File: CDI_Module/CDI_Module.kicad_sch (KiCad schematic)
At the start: 5 parts, among them Q1 TIC226

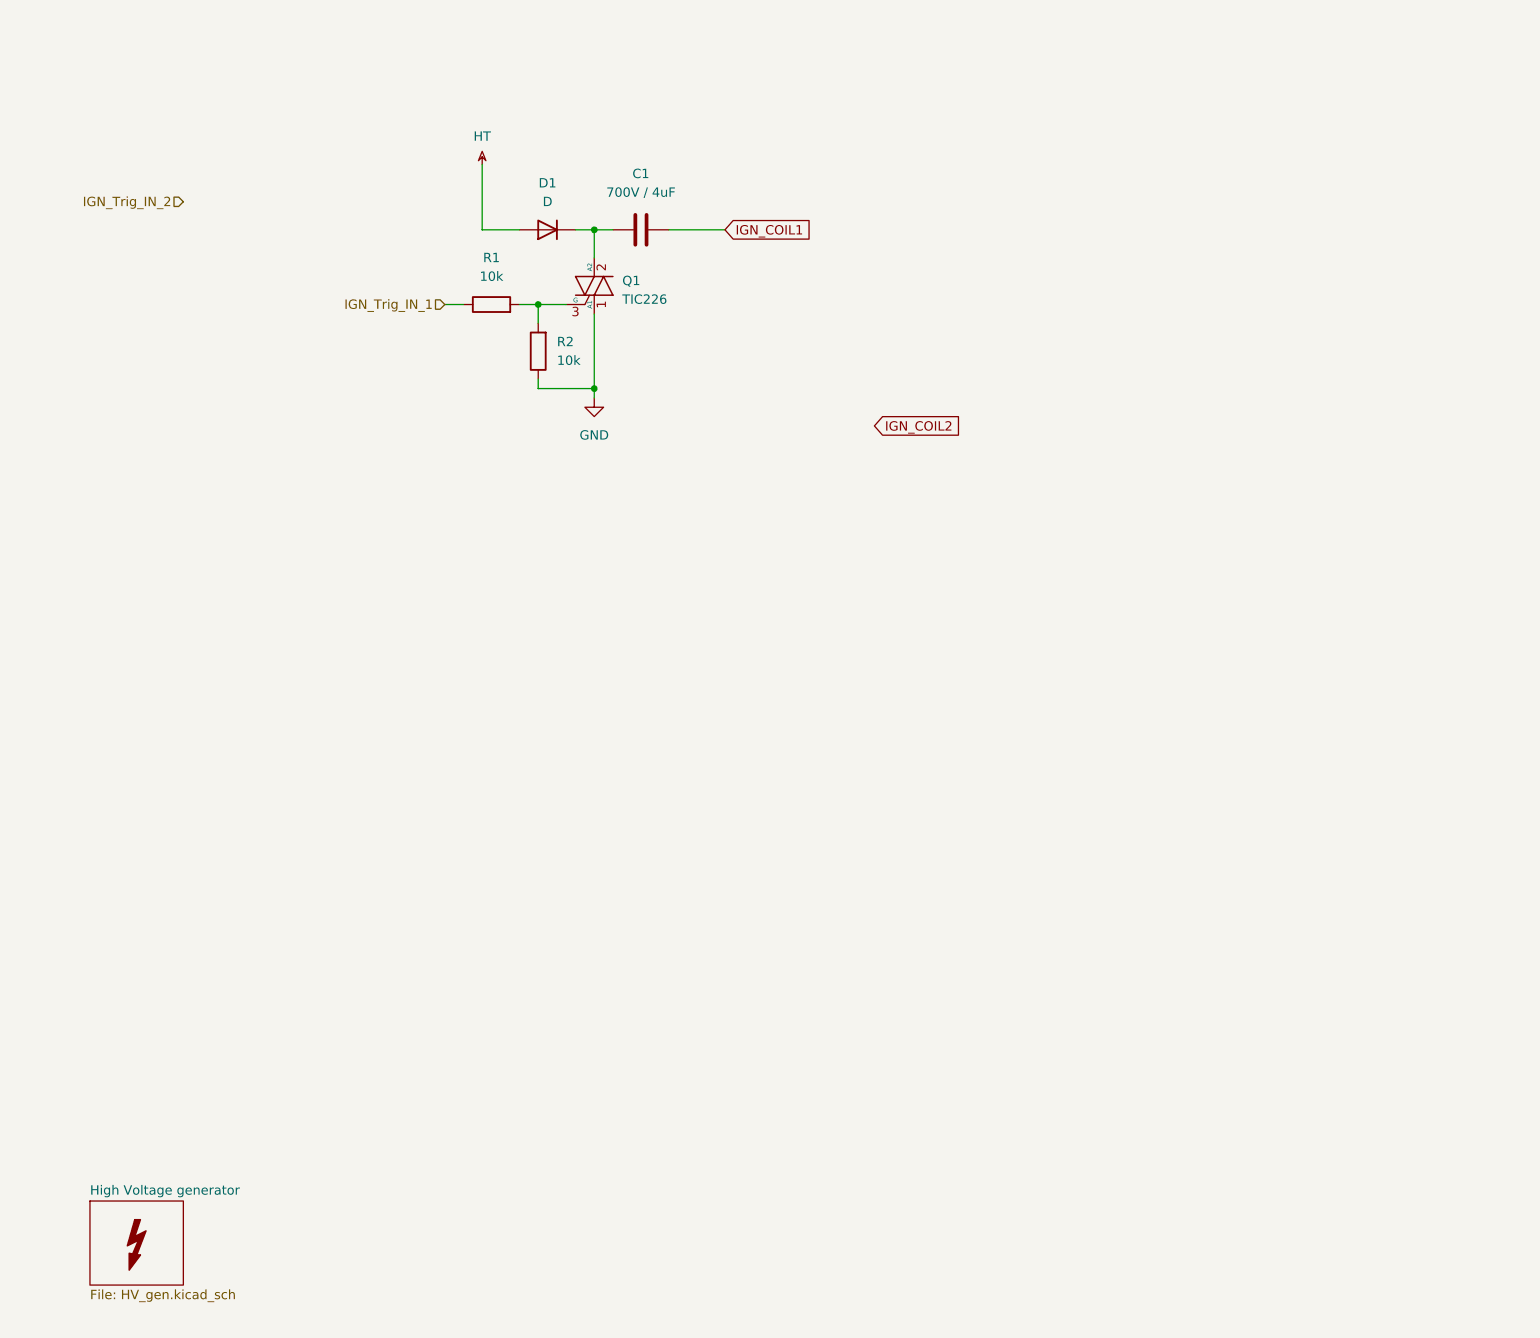
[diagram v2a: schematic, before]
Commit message: Changed Connectors for Molex CMC 48pins Black.
Changed ECU Connector for Molex CMC 48pins Black, for compacity and cost reduction. Designed custom Footprint for this purpose
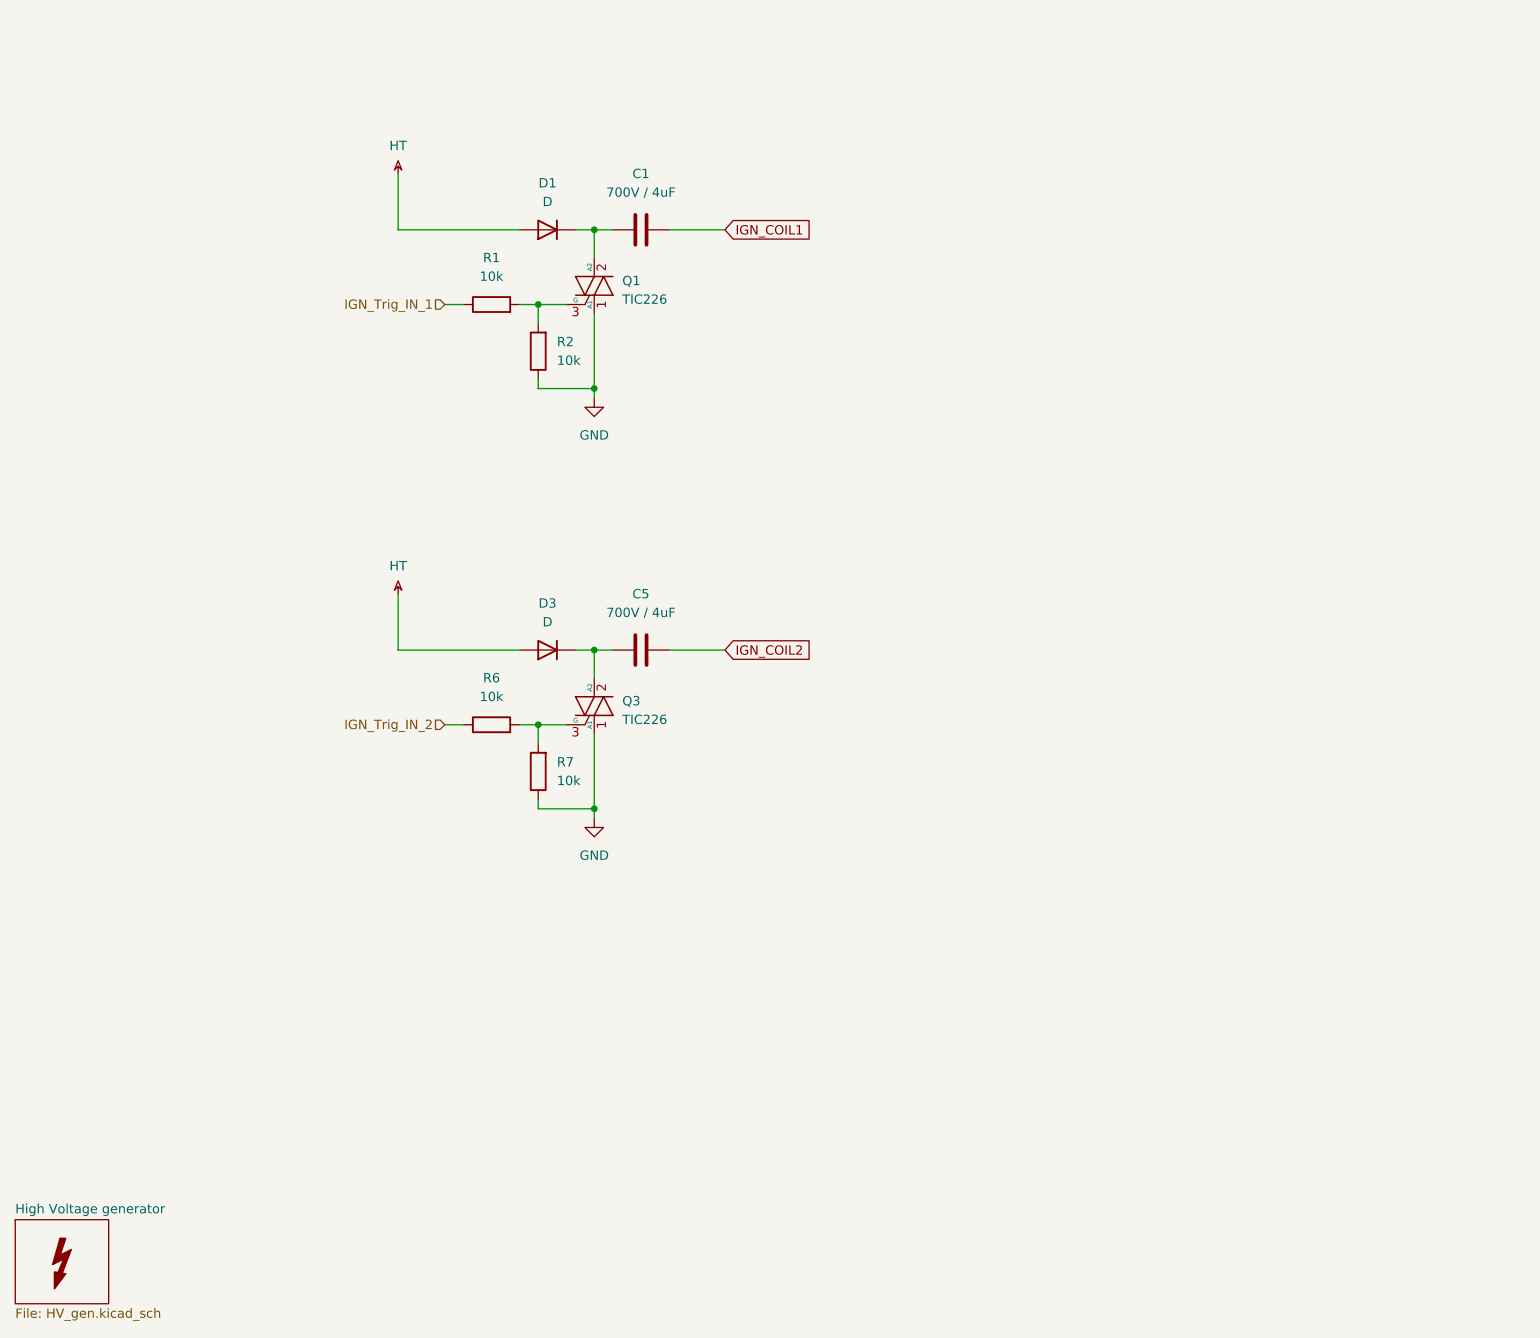
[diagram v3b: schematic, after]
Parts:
- added C5: 700V / 4uF, symbol Device:C
- added D3: D, Diode_SMD:D_0805_2012Metric_Pad1.15x1.40mm_HandSolder, symbol Device:D
- added Q3: TIC226, Package_TO_SOT_THT:TO-220-3_Vertical, symbol Triac_Thyristor:TIC226
- added R6, R7: 10k, Resistor_SMD:R_0603_1608Metric_Pad0.98x0.95mm_HandSolder, symbol Device:R
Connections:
- net GND: now also Q3.1 (A1), R7.1
- net HT: now also D3.2 (A)
- net IGN_COIL2: now also C5.2
- net IGN_Trig_IN_2: now also R6.1
- new net: C5.1, D3.1 (K), Q3.2 (A2)
- new net: Q3.3 (G), R6.2, R7.2

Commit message: Redraw CDI pwr Supply with Boost circuit for 48v output
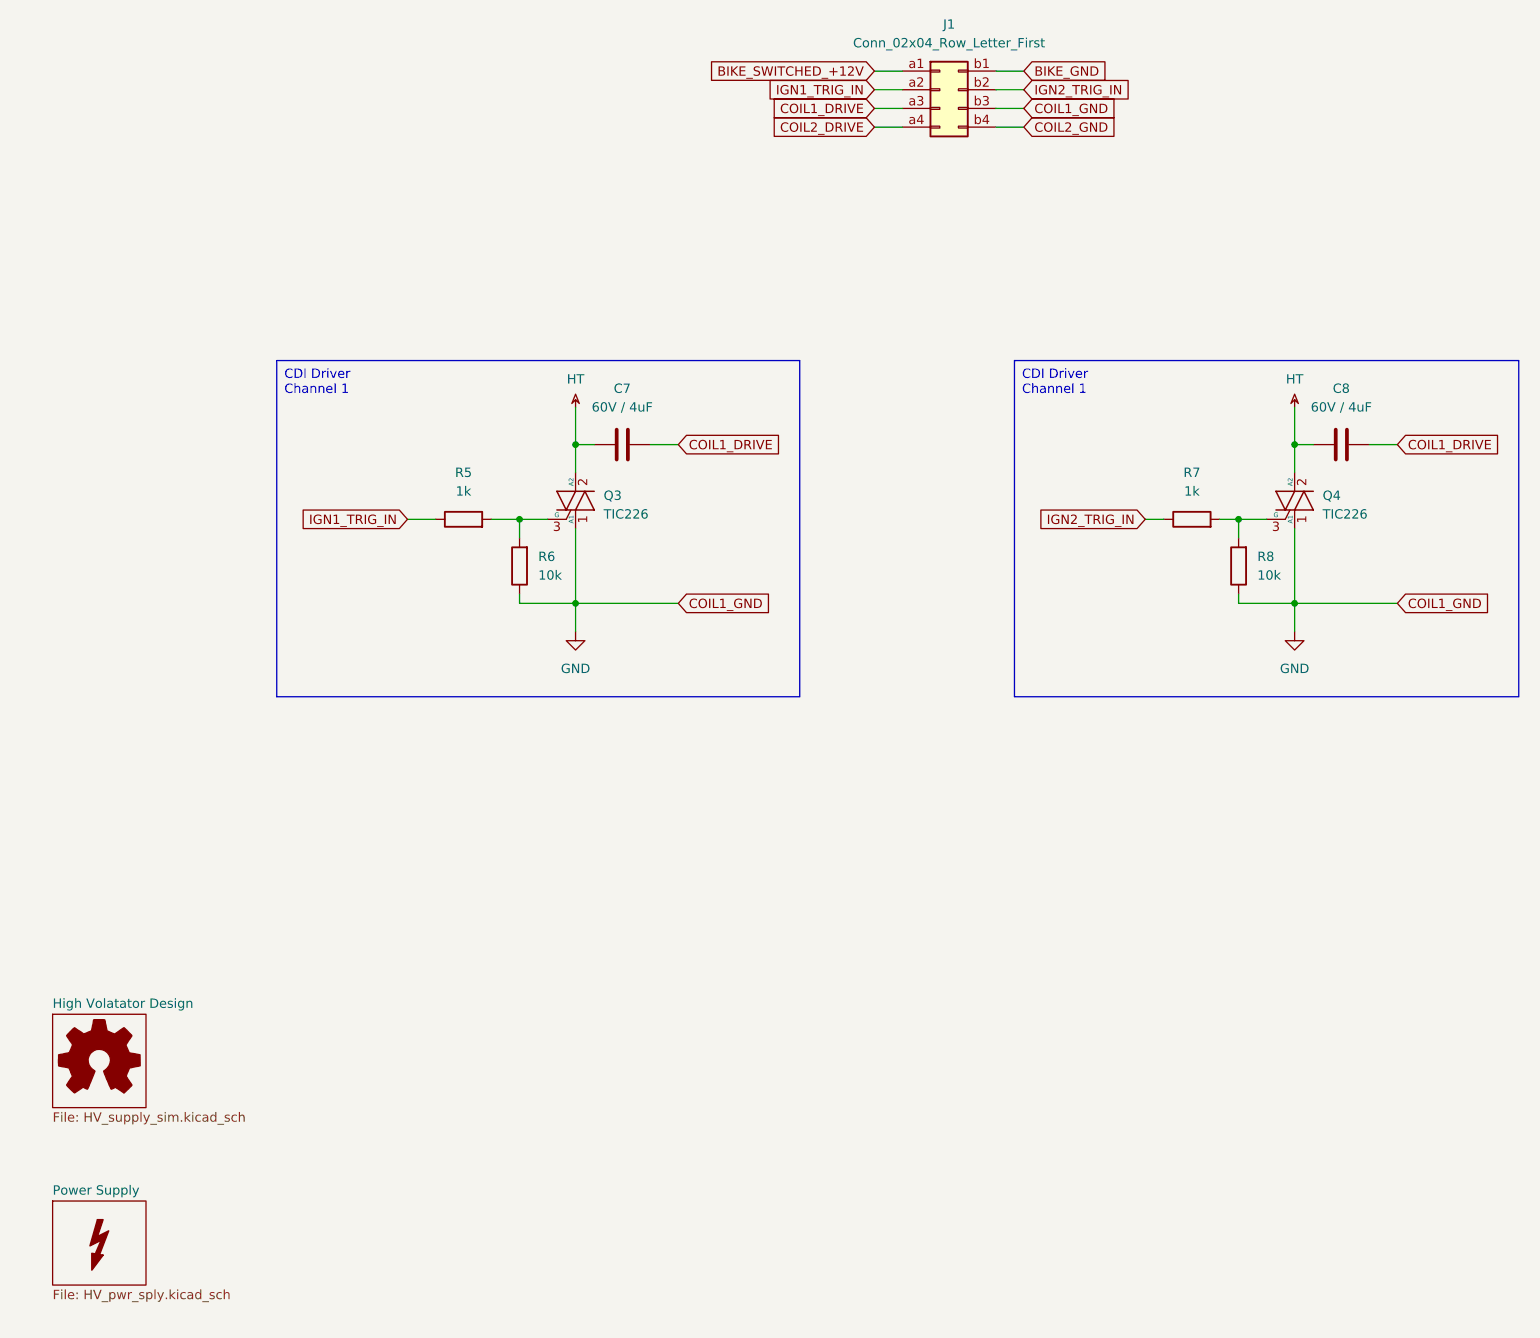
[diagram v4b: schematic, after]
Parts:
- removed C1, C5: 700V / 4uF, symbol Device:C
- removed D1, D3: D, Diode_SMD:D_0805_2012Metric_Pad1.15x1.40mm_HandSolder, symbol Device:D
- removed Q1: TIC226, Package_TO_SOT_THT:TO-220-3_Vertical, symbol Triac_Thyristor:TIC226
- removed R1, R2: 10k, Resistor_SMD:R_0603_1608Metric_Pad0.98x0.95mm_HandSolder, symbol Device:R
- added C7, C8: 60V / 4uF, Capacitor_THT:C_Rect_L7.0mm_W2.5mm_P5.00mm, symbol Device:C
- added J1: Conn_02x04_Row_Letter_First, Connector_Molex:Molex_Mega-Fit_76825-0008_2x04_P5.70mm_Horizontal, symbol Connector_Generic:Conn_02x04_Row_Letter_First
- added Q4: TIC226, Package_TO_SOT_THT:TO-220-3_Vertical, symbol Triac_Thyristor:TIC226
- added R5: 1k, Resistor_THT:R_Axial_DIN0207_L6.3mm_D2.5mm_P7.62mm_Horizontal, symbol Device:R
- added R8: 10k, Resistor_THT:R_Axial_DIN0207_L6.3mm_D2.5mm_P7.62mm_Horizontal, symbol Device:R
- R6: footprint Resistor_SMD:R_0603_1608Metric_Pad0.98x0.95mm_HandSolder -> Resistor_THT:R_Axial_DIN0207_L6.3mm_D2.5mm_P7.62mm_Horizontal
- R7: value 10k -> 1k; footprint Resistor_SMD:R_0603_1608Metric_Pad0.98x0.95mm_HandSolder -> Resistor_THT:R_Axial_DIN0207_L6.3mm_D2.5mm_P7.62mm_Horizontal
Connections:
- net IGN_Trig_IN_2 is gone; now on net GND: R6.1
- net GND: now also J1.b3 (Pin_b3), Q4.1 (A1), R8.1; no longer R7.1
- net HT: now also Q3.2 (A2), C7.1, C8.1, Q4.2 (A2)
- net at Q3.3 (G), R6.2: now also R5.2; no longer R7.2
- new net: Q4.3 (G), R7.2, R8.2
- new net BIKE_GND: J1.b1 (Pin_b1)
- new net BIKE_SWITCHED_+12V: J1.a1 (Pin_a1)
- new net COIL1_DRIVE: C7.2, C8.2, J1.a3 (Pin_a3)
- new net COIL2_DRIVE: J1.a4 (Pin_a4)
- new net COIL2_GND: J1.b4 (Pin_b4)
- new net IGN1_TRIG_IN: J1.a2 (Pin_a2), R5.1
- new net IGN2_TRIG_IN: J1.b2 (Pin_b2), R7.1
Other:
- sheet High Voltage generator renamed Power Supply
- added sheet High Volatator Design (HV_supply_sim.kicad_sch)
- sheet Power Supply: file HV_gen.kicad_sch -> HV_pwr_sply.kicad_sch

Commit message: Work in progress
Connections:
- net IGN2_TRIG_IN: now also R8.2
- net at Q4.3 (G), R7.2: no longer R8.2
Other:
- moved on the sheet: R7, R8
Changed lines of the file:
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@@
 	(paper "A4")
+	(junction
+		(at 176.53 85.09)
+		(diameter 0)
+		(color 0 0 0 0)
+	)
 	(junction
 		(at 194.31 96.52)
@@
 	)
 	(junction
-		(at 186.69 85.09)
-		(diameter 0)
-		(color 0 0 0 0)
-	)
-	(junction
 		(at 194.31 74.93)
 		(diameter 0)
@@
 	(wire
 		(pts
-			(xy 186.69 95.25) (xy 186.69 96.52)
+			(xy 176.53 95.25) (xy 176.53 96.52)
 		)
 		(stroke
@@
 	(wire
 		(pts
-			(xy 184.15 85.09) (xy 186.69 85.09)
-		)
-		(stroke
-			(width 0)
-			(type default)
-		)
-	)
-	(wire
-		(pts
 			(xy 194.31 86.36) (xy 194.31 96.52)
 		)
@@
 	(wire
 		(pts
+			(xy 187.96 85.09) (xy 190.5 85.09)
+		)
+		(stroke
+			(width 0)
+			(type default)
+		)
+	)
+	(wire
+		(pts
 			(xy 96.52 96.52) (xy 110.49 96.52)
 		)
@@
 	(wire
 		(pts
+			(xy 176.53 85.09) (xy 180.34 85.09)
+		)
+		(stroke
+			(width 0)
+			(type default)
+		)
+	)
+	(wire
+		(pts
 			(xy 194.31 74.93) (xy 194.31 78.74)
 		)
@@
 	(wire
 		(pts
-			(xy 186.69 96.52) (xy 194.31 96.52)
-		)
-		(stroke
-			(width 0)
-			(type default)
-		)
-	)
-	(wire
-		(pts
-			(xy 186.69 85.09) (xy 190.5 85.09)
+			(xy 176.53 96.52) (xy 194.31 96.52)
 		)
 		(stroke
@@
 	(wire
 		(pts
-			(xy 186.69 85.09) (xy 186.69 87.63)
+			(xy 176.53 85.09) (xy 176.53 87.63)
 		)
 		(stroke
@@
 	(symbol
 		(lib_id "Device:R")
-		(at 180.34 85.09 90)
+		(at 184.15 85.09 90)
 		(unit 1)
 		(exclude_from_sim yes)
@@
 		(fields_autoplaced yes)
 		(property "Reference" "R7"
-			(at 180.34 78.74 90)
+			(at 184.15 78.74 90)
 			(effects
 				(font
@@
 		)
 		(property "Value" "1k"
-			(at 180.34 81.28 90)
+			(at 184.15 81.28 90)
 			(effects
 				(font
@@
 		)
 		(property "Footprint" "Resistor_THT:R_Axial_DIN0207_L6.3mm_D2.5mm_P7.62mm_Horizontal"
-			(at 180.34 86.868 90)
+			(at 184.15 86.868 90)
 			(effects
 				(font
@@
 		)
 		(property "Datasheet" "~"
-			(at 180.34 85.09 0)
+			(at 184.15 85.09 0)
 			(effects
 				(font
@@
 		)
 		(property "Description" "Resistor"
-			(at 180.34 85.09 0)
+			(at 184.15 85.09 0)
 			(effects
 				(font
@@
 	(symbol
 		(lib_id "Device:R")
-		(at 186.69 91.44 180)
+		(at 176.53 91.44 180)
 		(unit 1)
 		(exclude_from_sim yes)
@@
 		(fields_autoplaced yes)
 		(property "Reference" "R8"
-			(at 189.23 90.1699 0)
+			(at 179.07 90.1699 0)
 			(effects
 				(font
@@
 		)
 		(property "Value" "10k"
-			(at 189.23 92.7099 0)
+			(at 179.07 92.7099 0)
 			(effects
 				(font
@@
 		)
 		(property "Footprint" "Resistor_THT:R_Axial_DIN0207_L6.3mm_D2.5mm_P7.62mm_Horizontal"
-			(at 188.468 91.44 90)
+			(at 178.308 91.44 90)
 			(effects
 				(font
@@
 		)
 		(property "Datasheet" "~"
-			(at 186.69 91.44 0)
+			(at 176.53 91.44 0)
 			(effects
 				(font
@@
 		)
 		(property "Description" "Resistor"
-			(at 186.69 91.44 0)
-			(effects
-				(font
+			(at 176.53 91.44 0)
+			(effects
+				(font
